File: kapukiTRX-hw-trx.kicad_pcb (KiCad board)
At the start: 4 copper layers, 45.7 x 27.9 mm, 93 parts, among them J1 GPS, J10 Conn_01x01, J11 Conn_01x01, J12 Conn_01x01, J13 Conn_01x01, J14 Conn_01x01, J15 Conn_01x01, J16 Conn_01x01, J17 Conn_01x01, J18 Conn_01x01, J19 GND for the Servo connectors, J2 SWD, J20 CAN, J21 Conn_01x01, J22 Conn_01x01, J3 Conn_01x01, J4 Conn_01x01, J5 Conn_01x01, J6 Conn_01x01, J7 Conn_01x01, J8 Conn_01x01, J9 Conn_01x01, U1 STM32G474VE, U2 LP38693-3.3, U3 TXB0108PWR, U4 LP38693-5.0, U5 MCP2562-E-MF, U6 LP38693SD-3.3, U7 BNO055, U8 BMP388, Y1 16MHz, Y2 32.768kHz

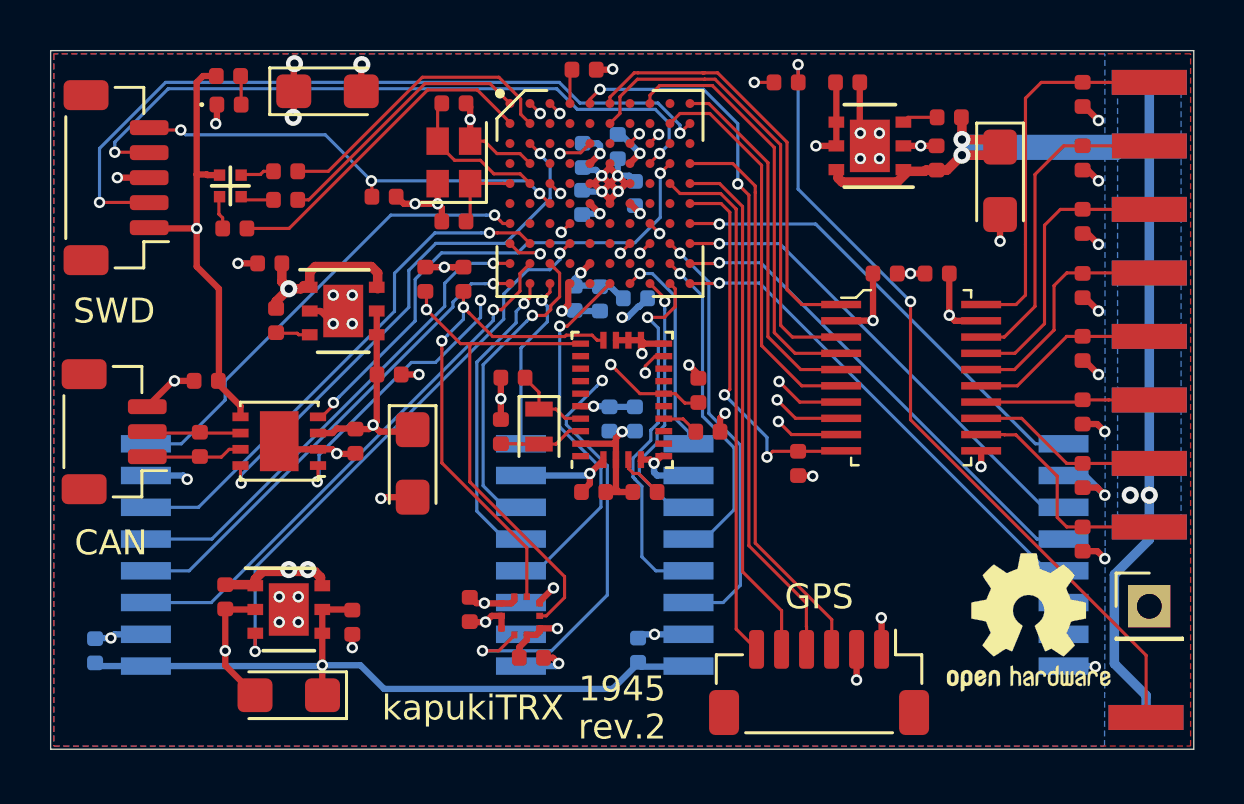
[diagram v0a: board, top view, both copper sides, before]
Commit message: Fix BMP388 footprint issue
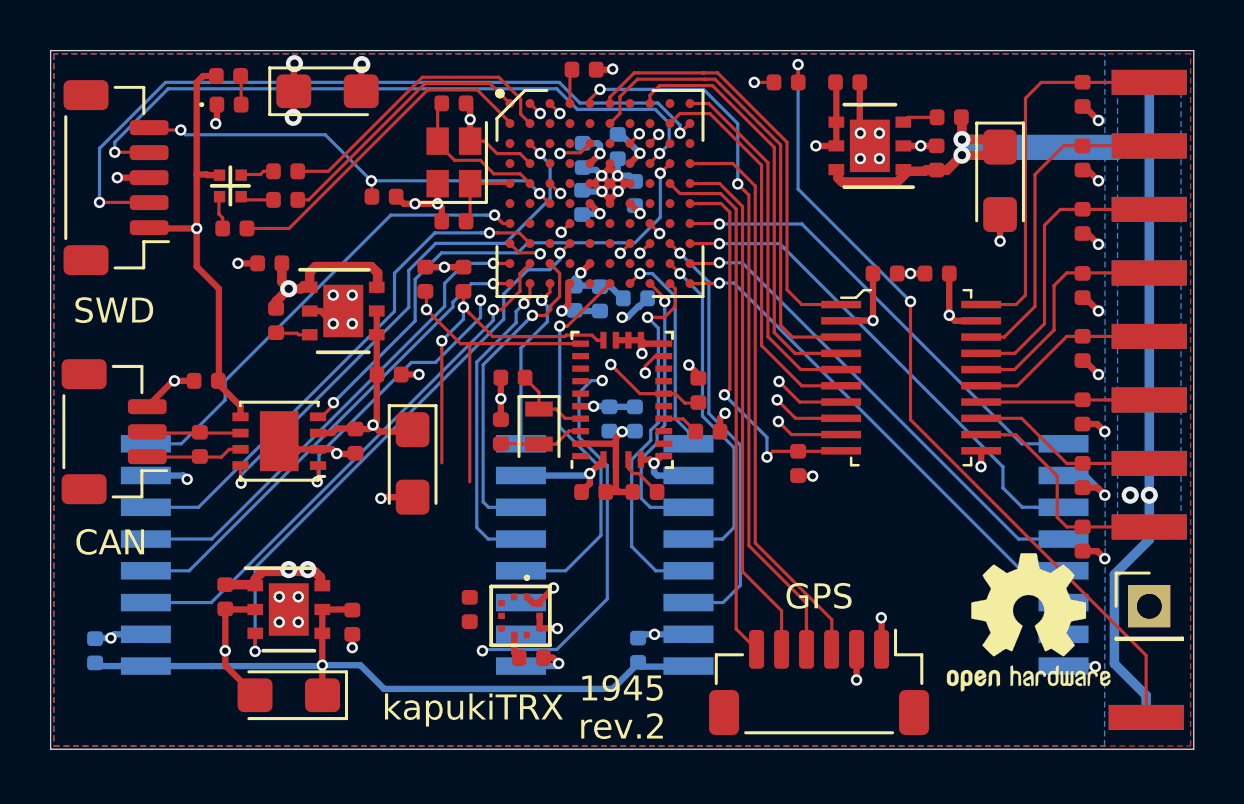
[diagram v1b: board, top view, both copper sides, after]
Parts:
- R6: value 2k2 -> 1k
- R7: value R -> 10k
- turned C33 to 90 degrees
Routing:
- net /SDA: track 31.7 -> 24.2 mm
- net /SCL: track 30.2 -> 23.4 mm
- net /VCCCPU: track 47.7 -> 45.7 mm, vias 16 -> 15
- net /BMPINT: track 25.7 -> 24.1 mm
- net GND: track 83.9 -> 82.4 mm, vias 58 -> 57
- net /RF2IRQ: track 14.9 -> 15.6 mm

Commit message: Fix BMP388 footprint issue
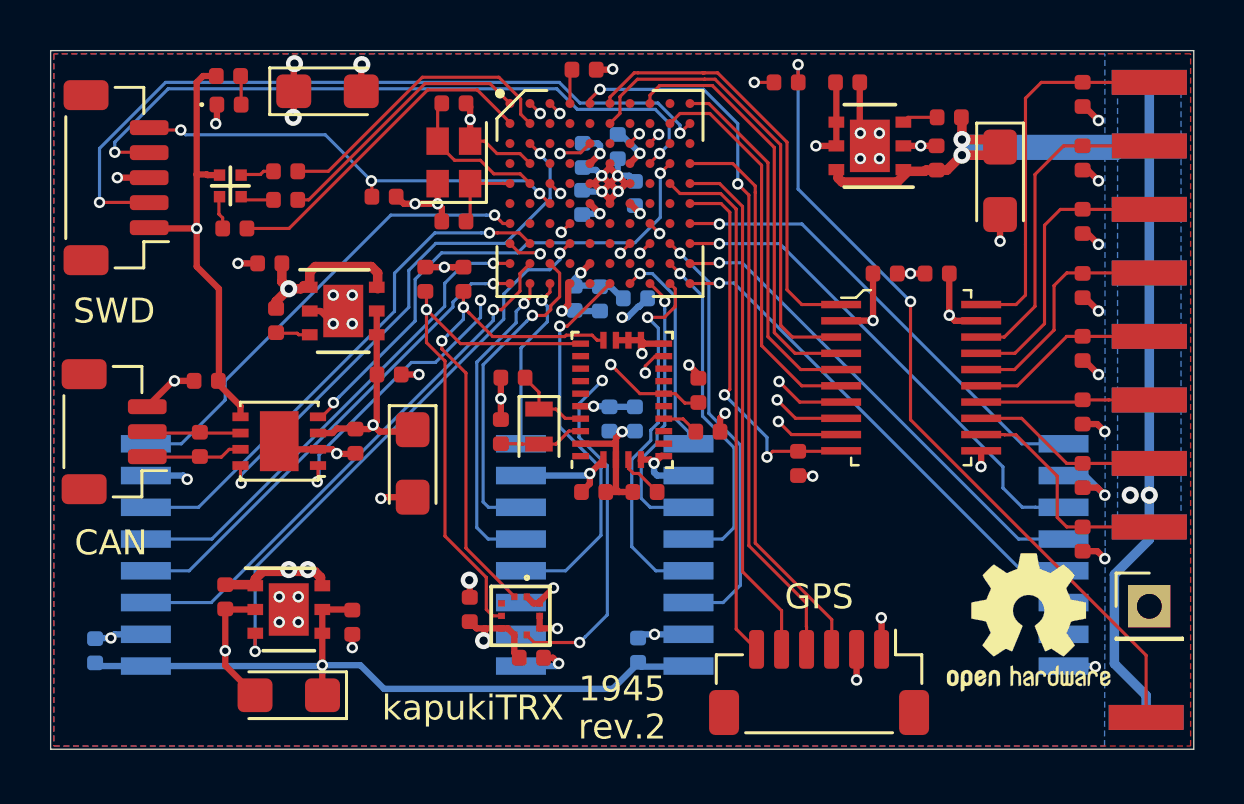
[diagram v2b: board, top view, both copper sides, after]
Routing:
- net /SDA: track 24.2 -> 32.3 mm
- net /SCL: track 23.4 -> 30.0 mm
- net /VCCCPU: track 45.7 -> 48.2 mm, vias 15 -> 16
- net /BMPINT: track 24.1 -> 22.4 mm
- net GND: track 82.4 -> 83.1 mm, vias 57 -> 58
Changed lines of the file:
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@@
     (thickness 1.6)
     (drawings 17)
-    (tracks 1028)
+    (tracks 1049)
     (zones 0)
     (modules 93)
@@
     (1 In1.Cu signal hide)
     (2 In2.Cu signal hide)
-    (31 B.Cu signal hide)
+    (31 B.Cu signal)
     (32 B.Adhes user hide)
     (33 F.Adhes user hide)
@@
   (segment (start 191.0085 117.086) (end 191.7112 117.086) (width 0.254) (layer F.Cu) (net 1))
   (segment (start 191.0085 117.086) (end 191.0085 116.586) (width 0.254) (layer F.Cu) (net 1))
+  (via (at 188.193856 115.158344) (size 0.6858) (drill 0.3302) (layers F.Cu B.Cu) (net 1))
+  (segment (start 188.214 115.847) (end 188.214 115.178488) (width 0.254) (layer F.Cu) (net 1))
+  (segment (start 188.214 115.178488) (end 188.193856 115.158344) (width 0.254) (layer F.Cu) (net 1))
   (via (at 198.196191 103.2764) (size 0.4572) (drill 0.254) (layers F.Cu B.Cu) (net 4))
   (segment (start 197.021 103.295) (end 198.177591 103.295) (width 0.127) (layer F.Cu) (net 4))
@@
   (segment (start 190.7585 116.086) (end 190.496 115.8235) (width 0.254) (layer F.Cu) (net 25))
   (segment (start 191.0085 116.086) (end 190.7585 116.086) (width 0.254) (layer F.Cu) (net 25))
+  (segment (start 188.214 116.817) (end 188.483 117.086) (width 0.254) (layer F.Cu) (net 25))
+  (segment (start 189.7335 117.086) (end 189.996 117.3485) (width 0.254) (layer F.Cu) (net 25))
+  (segment (start 189.4835 117.086) (end 189.7335 117.086) (width 0.254) (layer F.Cu) (net 25))
+  (via (at 188.765938 117.5766) (size 0.6858) (drill 0.3302) (layers F.Cu B.Cu) (net 25))
+  (segment (start 188.8156 117.526938) (end 188.765938 117.5766) (width 0.254) (layer F.Cu) (net 25))
+  (segment (start 188.8156 117.086) (end 188.8156 117.526938) (width 0.254) (layer F.Cu) (net 25))
+  (segment (start 188.8156 117.086) (end 189.4835 117.086) (width 0.254) (layer F.Cu) (net 25))
+  (segment (start 188.483 117.086) (end 188.8156 117.086) (width 0.254) (layer F.Cu) (net 25))
   (segment (start 178.435 115.339) (end 179.682 115.339) (width 0.381) (layer F.Cu) (net 26))
   (segment (start 179.635 115.113338) (end 179.940338 114.808) (width 0.381) (layer F.Cu) (net 26))
@@
   (via (at 191.0334 96.4946) (size 0.4572) (drill 0.254) (layers F.Cu B.Cu) (net 118))
   (segment (start 190.621 96.095) (end 190.6338 96.095) (width 0.127) (layer F.Cu) (net 118))
-  (segment (start 188.214 111.2266) (end 188.214 105.791) (width 0.127) (layer F.Cu) (net 118))
   (segment (start 192.6475 105.7) (end 188.123 105.7) (width 0.127) (layer F.Cu) (net 118))
-  (segment (start 188.214 105.7106) (end 188.2246 105.7) (width 0.127) (layer F.Cu) (net 118))
-  (segment (start 188.214 105.791) (end 188.214 105.7106) (width 0.127) (layer F.Cu) (net 118))
   (segment (start 188.2542 105.7) (end 188.2246 105.7) (width 0.127) (layer F.Cu) (net 118))
   (segment (start 186.4614 103.5558) (end 186.482544 103.576944) (width 0.127) (layer F.Cu) (net 118))
@@
   (segment (start 187.8436 105.7) (end 186.482544 104.338944) (width 0.127) (layer F.Cu) (net 118))
   (segment (start 188.2246 105.7) (end 187.8436 105.7) (width 0.127) (layer F.Cu) (net 118))
+  (segment (start 186.482544 104.662233) (end 186.482544 104.338944) (width 0.127) (layer F.Cu) (net 118))
+  (segment (start 186.482544 105.656457) (end 186.482544 104.662233) (width 0.127) (layer F.Cu) (net 118))
+  (segment (start 189.1284 116.586) (end 188.8744 116.332) (width 0.127) (layer F.Cu) (net 118))
+  (segment (start 189.4835 116.586) (end 189.1284 116.586) (width 0.127) (layer F.Cu) (net 118))
+  (segment (start 188.8744 116.332) (end 188.8744 115.048624) (width 0.127) (layer F.Cu) (net 118))
+  (segment (start 188.8744 115.048624) (end 187.2234 113.397624) (width 0.127) (layer F.Cu) (net 118))
+  (segment (start 187.2234 113.397624) (end 187.2234 106.397313) (width 0.127) (layer F.Cu) (net 118))
+  (segment (start 187.2234 106.397313) (end 186.482544 105.656457) (width 0.127) (layer F.Cu) (net 118))
   (via (at 191.8208 96.4946) (size 0.4572) (drill 0.254) (layers F.Cu B.Cu) (net 119))
   (segment (start 191.4212 96.095) (end 191.8208 96.4946) (width 0.127) (layer F.Cu) (net 119))
@@
   (segment (start 187.96 104.2416) (end 187.96 103.6066) (width 0.127) (layer F.Cu) (net 119))
   (segment (start 187.96 104.2416) (end 187.96 104.7242) (width 0.127) (layer B.Cu) (net 119))
-  (segment (start 187.0964 110.468224) (end 187.0964 105.911089) (width 0.127) (layer F.Cu) (net 119))
   (segment (start 187.96 104.7242) (end 187.324999 105.359201) (width 0.127) (layer B.Cu) (net 119))
   (segment (start 187.324999 105.359201) (end 187.0964 105.5878) (width 0.127) (layer B.Cu) (net 119))
-  (segment (start 187.0964 105.911089) (end 187.0964 105.5878) (width 0.127) (layer F.Cu) (net 119))
   (via (at 187.0964 105.5878) (size 0.4572) (drill 0.254) (layers F.Cu B.Cu) (net 119))
   (segment (start 192.071589 105.3592) (end 192.013924 105.416865) (width 0.127) (layer F.Cu) (net 119))
@@
   (segment (start 189.135265 105.416865) (end 188.188599 104.470199) (width 0.127) (layer F.Cu) (net 119))
   (segment (start 193.56 105.5625) (end 193.306 105.5625) (width 0.127) (layer F.Cu) (net 119))
+  (segment (start 187.0964 105.911089) (end 188.0616 106.876289) (width 0.127) (layer F.Cu) (net 119))
+  (segment (start 187.0964 105.5878) (end 187.0964 105.911089) (width 0.127) (layer F.Cu) (net 119))
+  (segment (start 189.996 115.811) (end 189.996 115.8235) (width 0.127) (layer F.Cu) (net 119))
+  (segment (start 188.0616 113.8766) (end 189.996 115.811) (width 0.127) (layer F.Cu) (net 119))
+  (segment (start 188.0616 106.876289) (end 188.0616 113.8766) (width 0.127) (layer F.Cu) (net 119))
   (segment (start 196.437 107.7) (end 196.814 108.077) (width 0.127) (layer F.Cu) (net 120))
   (segment (start 195.9725 107.7) (end 196.437 107.7) (width 0.127) (layer F.Cu) (net 120))
@@
   (segment (start 195.421 100.895) (end 195.421 100.9076) (width 0.127) (layer F.Cu) (net 122))
   (segment (start 195.421 100.9076) (end 195.8086 101.2952) (width 0.127) (layer F.Cu) (net 122))
-  (via (at 188.722 117.983) (size 0.4572) (drill 0.254) (layers F.Cu B.Cu) (net 122))
   (segment (start 193.284033 106.947786) (end 193.512632 107.176385) (width 0.127) (layer In2.Cu) (net 122))
   (segment (start 195.8086 101.2952) (end 194.40093 101.2952) (width 0.127) (layer In2.Cu) (net 122))
@@
   (segment (start 194.40093 101.2952) (end 193.577406 102.118724) (width 0.127) (layer In2.Cu) (net 122))
   (segment (start 193.284033 106.448155) (end 193.284033 106.947786) (width 0.127) (layer In2.Cu) (net 122))
-  (segment (start 193.077015 107.176385) (end 193.512632 107.176385) (width 0.127) (layer B.Cu) (net 122))
-  (segment (start 192.5828 107.6706) (end 193.077015 107.176385) (width 0.127) (layer B.Cu) (net 122))
-  (segment (start 188.7728 117.9322) (end 191.6938 117.9322) (width 0.127) (layer B.Cu) (net 122))
-  (segment (start 188.722 117.983) (end 188.7728 117.9322) (width 0.127) (layer B.Cu) (net 122))
-  (segment (start 191.6938 117.9322) (end 193.714679 115.911321) (width 0.127) (layer B.Cu) (net 122))
-  (segment (start 193.714679 115.911321) (end 193.714679 110.576257) (width 0.127) (layer B.Cu) (net 122))
-  (segment (start 193.714679 110.576257) (end 192.5828 109.444378) (width 0.127) (layer B.Cu) (net 122))
-  (segment (start 192.5828 109.444378) (end 192.5828 107.6706) (width 0.127) (layer B.Cu) (net 122))
+  (via (at 192.6082 117.652799) (size 0.4572) (drill 0.254) (layers F.Cu B.Cu) (net 122))
+  (segment (start 190.496 117.3485) (end 190.496 117.361) (width 0.127) (layer F.Cu) (net 122))
+  (segment (start 193.714679 110.576257) (end 193.714679 116.54632) (width 0.127) (layer B.Cu) (net 122))
+  (segment (start 190.496 117.361) (end 190.787799 117.652799) (width 0.127) (layer F.Cu) (net 122))
+  (segment (start 192.836799 117.4242) (end 192.6082 117.652799) (width 0.127) (layer B.Cu) (net 122))
+  (segment (start 192.5828 109.444378) (end 193.714679 110.576257) (width 0.127) (layer B.Cu) (net 122))
+  (segment (start 193.714679 116.54632) (end 192.836799 117.4242) (width 0.127) (layer B.Cu) (net 122))
+  (segment (start 192.5828 108.106217) (end 192.5828 109.444378) (width 0.127) (layer B.Cu) (net 122))
+  (segment (start 193.512632 107.176385) (end 192.5828 108.106217) (width 0.127) (layer B.Cu) (net 122))
+  (segment (start 192.284911 117.652799) (end 192.6082 117.652799) (width 0.127) (layer F.Cu) (net 122))
+  (segment (start 190.787799 117.652799) (end 192.284911 117.652799) (width 0.127) (layer F.Cu) (net 122))
   (via (at 179.07 111.2774) (size 0.4572) (drill 0.254) (layers F.Cu B.Cu) (net 123))
   (segment (start 179.044 110.576) (end 179.044 111.2514) (width 0.127) (layer F.Cu) (net 123))

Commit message: Final changes for rev.3
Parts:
- removed REF**: OSHW-Logo2_7.3x6mm_SilkScreen, Symbol:OSHW-Logo2_7.3x6mm_SilkScreen
- added R15: 0, Resistor_SMD:R_0402_1005Metric, F.Cu at (190.9, 94.7)
- added R16: 10k, Resistor_SMD:R_0402_1005Metric, F.Cu at (184.8, 100.9)
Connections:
- C5 pad 2: GND -> /VCCCPU
- R4 pad 2: GND -> /VCCCPU
- U1 pad C7: /RXTX -> Net-(R14-Pad2)
- U1 pad C8: Net-(R14-Pad2) -> /RXTX
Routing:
- net /VCCCPU: track 48.2 -> 52.0 mm, vias 16 -> 19
- net /SDA: track 32.3 -> 36.0 mm
- net /RXTX: track 40.6 -> 37.8 mm
- net /NRST: track 17.9 -> 19.0 mm
- net /TXMODE: track 1.39 -> 2.35 mm
- net Net-(R14-Pad2): track 6.07 -> 6.93 mm
- net GND: track 83.1 -> 82.9 mm, vias 58 -> 57
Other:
- board text added: "2001"
- board text added: "rev.3"
- board text removed: "1945"
- board text removed: "rev.2"

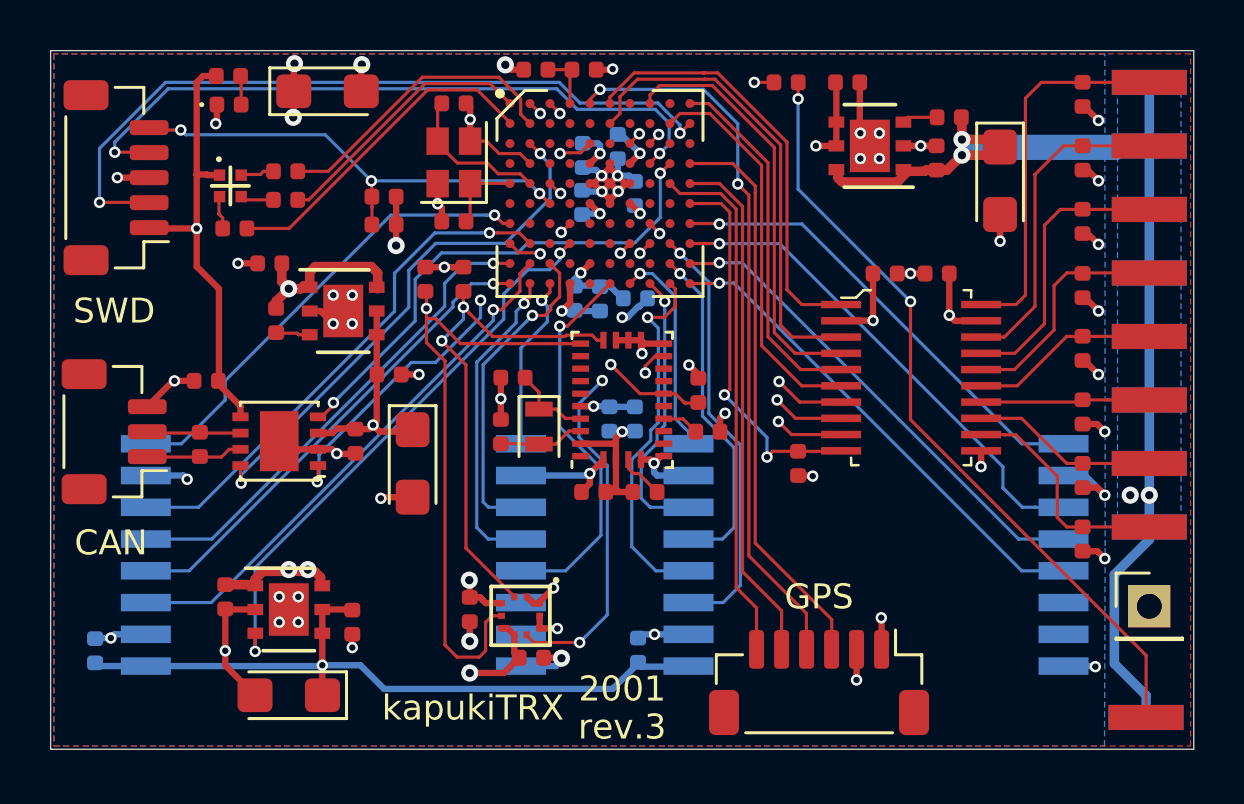
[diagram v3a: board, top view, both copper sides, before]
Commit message: Add boot resistor, and fix CAN RX pin
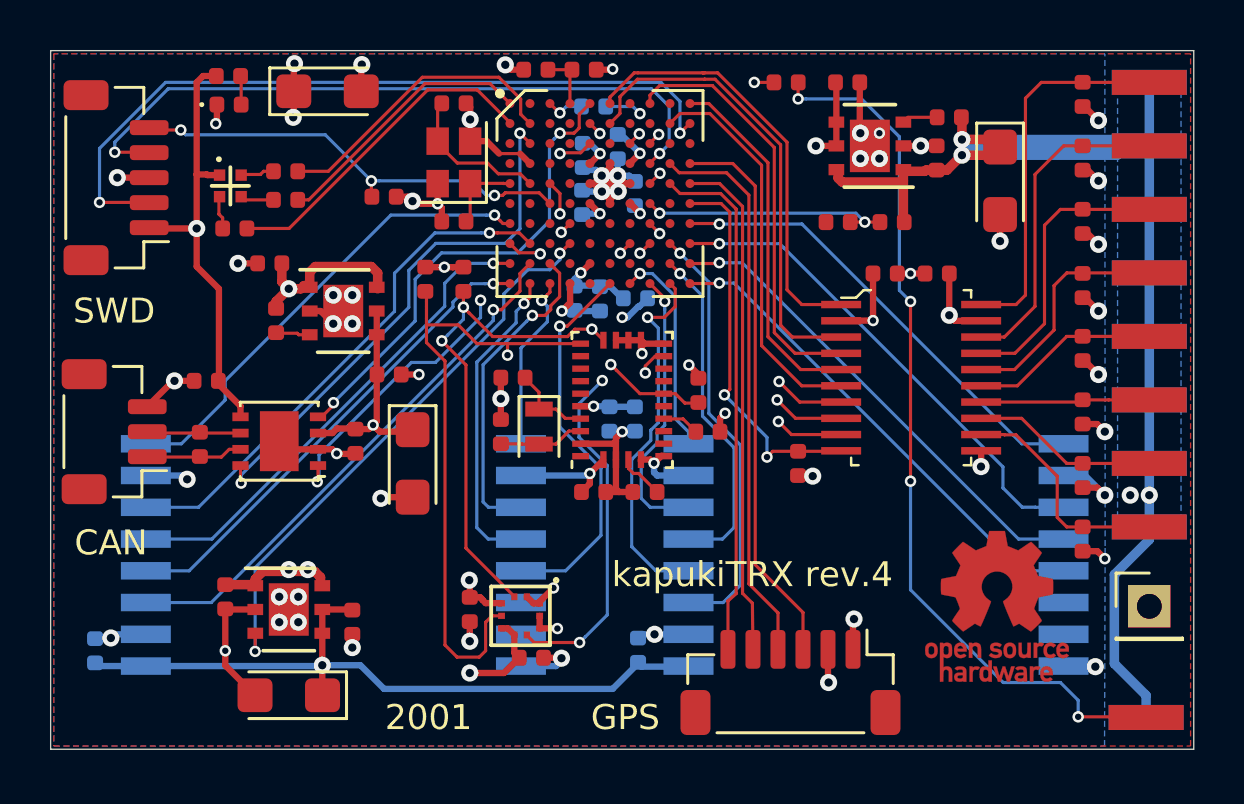
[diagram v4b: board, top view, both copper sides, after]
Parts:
- added R17: 10k, Resistor_SMD:R_0402_1005Metric, F.Cu at (202.9, 100.8)
- added R18: 10k, Resistor_SMD:R_0402_1005Metric, B.Cu at (193.2, 96.2)
- added REF**: OSHW-Logo_5.7x6mm_Copper, Symbol:OSHW-Logo_5.7x6mm_Copper, F.Cu at (209.3, 116.2)
- moved R16 20.3 mm to (205.1, 100.8)
- moved J1 1.14 mm to (201.0, 119.3)
- turned C5 to 180 degrees
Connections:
- net /CANEN renamed /CANSTBY
- C5 pad 1: /NRST -> GND
- C5 pad 2: /VCCCPU -> /NRST
- R16 pad 1: /NRST -> /UMEAS
- R16 pad 2: /VCCCPU -> IN
- U1 pad A2: /SDA -> Net-(U1-PadA2)
- U1 pad A3: /SCL -> Net-(R18-Pad2)
- U1 pad A5: /GPSRX -> /CANRX
- U1 pad B5: Net-(U1-PadB5) -> /SDA
- U1 pad D9: /CANRX -> /GPSRX
- U1 pad E8: Net-(U1-PadE8) -> /SCL
- U1 pad F8: Net-(U1-PadF8) -> /UMEAS
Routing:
- net /UMEAS: track 0.00 -> 10.1 mm, vias 0 -> 2
- net /GPSRX: track 29.0 -> 22.3 mm, vias 2 -> 0
- net /RXTX: track 37.8 -> 42.2 mm, vias 3 -> 5
- net GND: track 82.9 -> 86.2 mm, vias 57 -> 59
- net /VCCCPU: track 52.0 -> 49.8 mm, vias 19 -> 18
- net IN: track 153.1 -> 154.9 mm
- net /SCL: track 29.9 -> 28.1 mm, vias 3 -> 4
- net Net-(R18-Pad2): track 0.00 -> 1.52 mm, vias 0 -> 1
- net /CANRX: track 20.3 -> 19.2 mm
- net /NRST: track 19.0 -> 18.1 mm
- net /SWCLK: track 30.0 -> 30.6 mm
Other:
- board text added: "kapukiTRX rev.4"
- board text removed: "kapukiTRX"
- board text removed: "rev.3"
